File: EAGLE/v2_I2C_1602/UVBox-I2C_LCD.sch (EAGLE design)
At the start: 56 parts, among them IC1 ULN2003AD, Q1 16M, Q2 BC817, SW1 Start, SW2 Mode, SW3 Add, SW4 Sub, U1 7812DT, U2 7805DT

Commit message: 細微修改
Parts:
- added C12: 104, rcl:C-EUC0603
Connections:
- net N$29 renamed IC2P3
- removed net N$14: LCD.A, Q2.C
- new net LCD_A: LCD.A, Q2.E
- net +5V: now also C12.2
- net GND: now also C12.1, LCD.K; no longer Q2.E, VR1.E, VR2.E
- net KEY1: now also RN1D.1; no longer RN1A.1
- net KEY2: now also RN1C.1; no longer RN1B.1
- net KEY3: now also RN1B.1; no longer RN1C.1
- net KEY4: now also RN1A.1; no longer RN1D.1
- net N$12: now also Q2.C; no longer LCD.K
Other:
- moved on the sheet: C8, LCD, Q2, RN1A, RN1B, RN1C, RN1D, RN3A, VR1, VR2

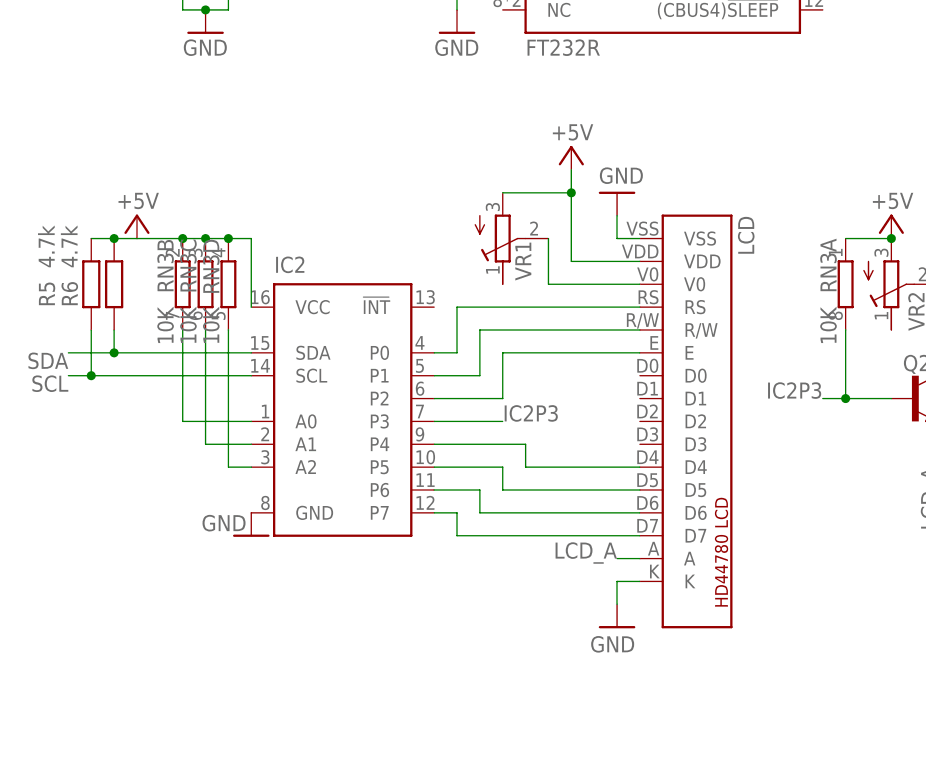
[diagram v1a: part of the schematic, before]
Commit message: 調整線路配置
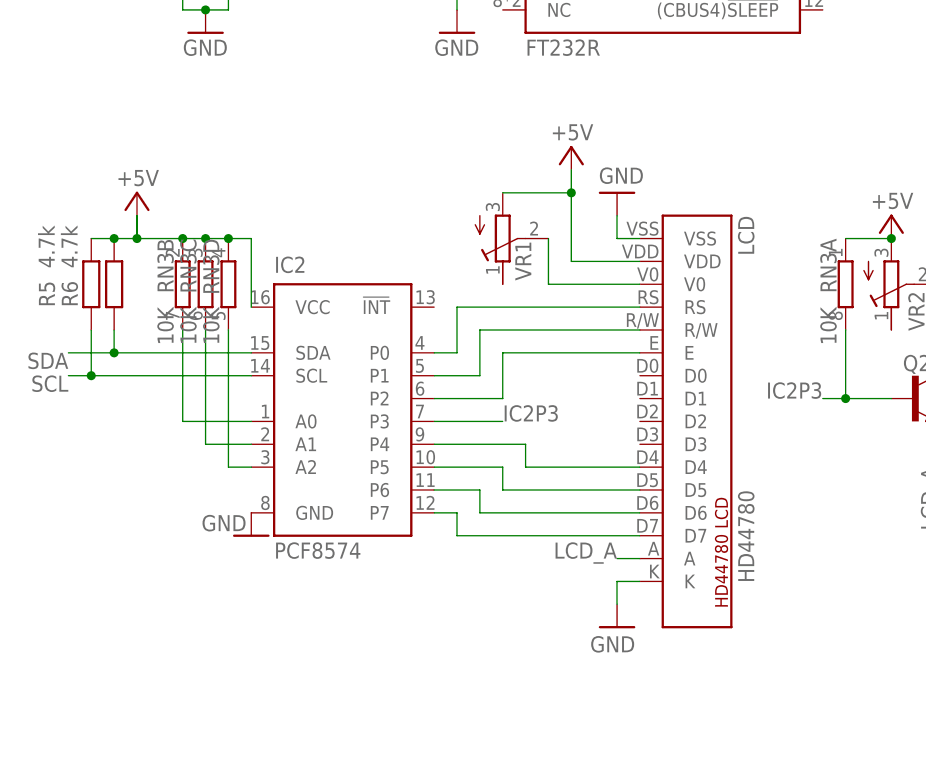
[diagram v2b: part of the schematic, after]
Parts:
- IC2: value (none) -> PCF8574
- LCD: value (none) -> HD44780
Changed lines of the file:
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@@
 <?xml version="1.0" encoding="utf-8"?>
 <!DOCTYPE eagle SYSTEM "eagle.dtd">
-<eagle version="8.4.2">
+<eagle version="8.5.2">
 <drawing>
 <settings>
-<setting alwaysvectorfont="yes"/>
+<setting alwaysvectorfont="no"/>
 <setting keepoldvectorfont="yes"/>
 <setting verticaltext="up"/>
@@
 <grid distance="0.1" unitdist="inch" unit="inch" style="lines" multiple="1" display="no" altdistance="0.01" altunitdist="inch" altunit="inch"/>
 <layers>
-<layer number="1" name="Top" color="4" fill="1" visible="yes" active="no"/>
-<layer number="2" name="Route2" color="1" fill="3" visible="yes" active="no"/>
-<layer number="3" name="Route3" color="4" fill="3" visible="yes" active="no"/>
-<layer number="4" name="Route4" color="1" fill="4" visible="yes" active="no"/>
-<layer number="5" name="Route5" color="4" fill="4" visible="yes" active="no"/>
-<layer number="6" name="Route6" color="1" fill="8" visible="yes" active="no"/>
-<layer number="7" name="Route7" color="4" fill="8" visible="yes" active="no"/>
-<layer number="8" name="Route8" color="1" fill="2" visible="yes" active="no"/>
-<layer number="9" name="Route9" color="4" fill="2" visible="yes" active="no"/>
-<layer number="10" name="Route10" color="1" fill="7" visible="yes" active="no"/>
-<layer number="11" name="Route11" color="4" fill="7" visible="yes" active="no"/>
-<layer number="12" name="Route12" color="1" fill="5" visible="yes" active="no"/>
-<layer number="13" name="Route13" color="4" fill="5" visible="yes" active="no"/>
-<layer number="14" name="Route14" color="1" fill="6" visible="yes" active="no"/>
-<layer number="15" name="Route15" color="4" fill="6" visible="yes" active="no"/>
-<layer number="16" name="Bottom" color="1" fill="1" visible="yes" active="no"/>
-<layer number="17" name="Pads" color="2" fill="1" visible="yes" active="no"/>
-<layer number="18" name="Vias" color="2" fill="1" visible="yes" active="no"/>
-<layer number="19" name="Unrouted" color="6" fill="1" visible="yes" active="no"/>
-<layer number="20" name="Dimension" color="15" fill="1" visible="yes" active="no"/>
-<layer number="21" name="tPlace" color="7" fill="1" visible="yes" active="no"/>
-<layer number="22" name="bPlace" color="7" fill="1" visible="yes" active="no"/>
-<layer number="23" name="tOrigins" color="15" fill="1" visible="yes" active="no"/>
-<layer number="24" name="bOrigins" color="15" fill="1" visible="yes" active="no"/>
-<layer number="25" name="tNames" color="7" fill="1" visible="yes" active="no"/>
-<layer number="26" name="bNames" color="7" fill="1" visible="yes" active="no"/>
-<layer number="27" name="tValues" color="7" fill="1" visible="yes" active="no"/>
-<layer number="28" name="bValues" color="7" fill="1" visible="yes" active="no"/>
+<layer number="1" name="Top" color="4" fill="1" visible="no" active="no"/>
+<layer number="2" name="Route2" color="1" fill="3" visible="no" active="no"/>
+<layer number="3" name="Route3" color="4" fill="3" visible="no" active="no"/>
+<layer number="4" name="Route4" color="1" fill="4" visible="no" active="no"/>
+<layer number="5" name="Route5" color="4" fill="4" visible="no" active="no"/>
+<layer number="6" name="Route6" color="1" fill="8" visible="no" active="no"/>
+<layer number="7" name="Route7" color="4" fill="8" visible="no" active="no"/>
+<layer number="8" name="Route8" color="1" fill="2" visible="no" active="no"/>
+<layer number="9" name="Route9" color="4" fill="2" visible="no" active="no"/>
+<layer number="10" name="Route10" color="1" fill="7" visible="no" active="no"/>
+<layer number="11" name="Route11" color="4" fill="7" visible="no" active="no"/>
+<layer number="12" name="Route12" color="1" fill="5" visible="no" active="no"/>
+<layer number="13" name="Route13" color="4" fill="5" visible="no" active="no"/>
+<layer number="14" name="Route14" color="1" fill="6" visible="no" active="no"/>
+<layer number="15" name="Route15" color="4" fill="6" visible="no" active="no"/>
+<layer number="16" name="Bottom" color="1" fill="1" visible="no" active="no"/>
+<layer number="17" name="Pads" color="2" fill="1" visible="no" active="no"/>
+<layer number="18" name="Vias" color="2" fill="1" visible="no" active="no"/>
+<layer number="19" name="Unrouted" color="6" fill="1" visible="no" active="no"/>
+<layer number="20" name="Dimension" color="15" fill="1" visible="no" active="no"/>
+<layer number="21" name="tPlace" color="7" fill="1" visible="no" active="no"/>
+<layer number="22" name="bPlace" color="7" fill="1" visible="no" active="no"/>
+<layer number="23" name="tOrigins" color="15" fill="1" visible="no" active="no"/>
+<layer number="24" name="bOrigins" color="15" fill="1" visible="no" active="no"/>
+<layer number="25" name="tNames" color="7" fill="1" visible="no" active="no"/>
+<layer number="26" name="bNames" color="7" fill="1" visible="no" active="no"/>
+<layer number="27" name="tValues" color="7" fill="1" visible="no" active="no"/>
+<layer number="28" name="bValues" color="7" fill="1" visible="no" active="no"/>
 <layer number="29" name="tStop" color="7" fill="3" visible="no" active="no"/>
 <layer number="30" name="bStop" color="7" fill="6" visible="no" active="no"/>
@@
 <layer number="35" name="tGlue" color="7" fill="4" visible="no" active="no"/>
 <layer number="36" name="bGlue" color="7" fill="5" visible="no" active="no"/>
-<layer number="37" name="tTest" color="7" fill="1" visible="yes" active="no"/>
-<layer number="38" name="bTest" color="7" fill="1" visible="yes" active="no"/>
+<layer number="37" name="tTest" color="7" fill="1" visible="no" active="no"/>
+<layer number="38" name="bTest" color="7" fill="1" visible="no" active="no"/>
 <layer number="39" name="tKeepout" color="4" fill="11" visible="no" active="no"/>
 <layer number="40" name="bKeepout" color="1" fill="11" visible="no" active="no"/>
@@
 <layer number="44" name="Drills" color="7" fill="1" visible="no" active="no"/>
 <layer number="45" name="Holes" color="7" fill="1" visible="no" active="no"/>
-<layer number="46" name="Milling" color="3" fill="1" visible="yes" active="no"/>
-<layer number="47" name="Measures" color="7" fill="1" visible="yes" active="no"/>
-<layer number="48" name="Document" color="7" fill="1" visible="yes" active="no"/>
-<layer number="49" name="Reference" color="7" fill="1" visible="yes" active="no"/>
-<layer number="50" name="dxf" color="7" fill="1" visible="yes" active="no"/>
-<layer number="51" name="tDocu" color="7" fill="1" visible="yes" active="no"/>
-<layer number="52" name="bDocu" color="7" fill="1" visible="yes" active="no"/>
-<layer number="53" name="tGND_GNDA" color="7" fill="9" visible="yes" active="no"/>
-<layer number="54" name="bGND_GNDA" color="1" fill="9" visible="yes" active="no"/>
-<layer number="56" name="wert" color="7" fill="1" visible="yes" active="no"/>
-<layer number="57" name="tCAD" color="7" fill="1" visible="yes" active="no"/>
+<layer number="46" name="Milling" color="3" fill="1" visible="no" active="no"/>
+<layer number="47" name="Measures" color="7" fill="1" visible="no" active="no"/>
+<layer number="48" name="Document" color="7" fill="1" visible="no" active="no"/>
+<layer number="49" name="Reference" color="7" fill="1" visible="no" active="no"/>
+<layer number="50" name="dxf" color="7" fill="1" visible="no" active="no"/>
+<layer number="51" name="tDocu" color="7" fill="1" visible="no" active="no"/>
+<layer number="52" name="bDocu" color="7" fill="1" visible="no" active="no"/>
+<layer number="53" name="tGND_GNDA" color="7" fill="9" visible="no" active="no"/>
+<layer number="54" name="bGND_GNDA" color="1" fill="9" visible="no" active="no"/>
+<layer number="56" name="wert" color="7" fill="1" visible="no" active="no"/>
+<layer number="57" name="tCAD" color="7" fill="1" visible="no" active="no"/>
 <layer number="90" name="Modules" color="5" fill="1" visible="no" active="no"/>
 <layer number="91" name="Nets" color="2" fill="1" visible="yes" active="yes"/>
@@
 <part name="GND11" library="supply1" deviceset="GND" device=""/>
 <part name="D9" library="led" deviceset="LED" device="CHIPLED_1206" value="Red"/>
-<part name="LCD" library="0_MyCustom" deviceset="LCD-HD44780" device="-1602"/>
-<part name="IC2" library="0_MyIC" deviceset="PCF8574" device="/SO16W"/>
+<part name="LCD" library="0_MyCustom" deviceset="LCD-HD44780" device="-1602" value="HD44780"/>
+<part name="IC2" library="0_MyIC" deviceset="PCF8574" device="/SO16W" value="PCF8574"/>
 <part name="P+11" library="supply1" deviceset="+5V" device=""/>
 <part name="RN3" library="0_MyCustom" deviceset="RN4R" device="-CAY16" value="10K"/>
@@
 <attribute name="VALUE" x="132.334" y="97.282" size="1.778" layer="96"/>
 </instance>
-<instance part="P+1" gate="1" x="20.32" y="63.5" smashed="yes">
-<attribute name="VALUE" x="18.034" y="64.262" size="1.778" layer="96"/>
+<instance part="P+1" gate="1" x="20.32" y="66.04" smashed="yes">
+<attribute name="VALUE" x="18.034" y="66.802" size="1.778" layer="96"/>
 </instance>
 <instance part="P+10" gate="1" x="246.38" y="91.44" smashed="yes">
@@
 <pinref part="R6" gate="G$1" pin="1"/>
 <wire x1="17.78" y1="60.96" x2="20.32" y2="60.96" width="0.1524" layer="91"/>
+<wire x1="20.32" y1="60.96" x2="20.32" y2="63.5" width="0.1524" layer="91"/>
 <junction x="17.78" y="60.96"/>
 <pinref part="R5" gate="G$1" pin="1"/>
@@
 <junction x="30.48" y="60.96"/>
 <wire x1="25.4" y1="60.96" x2="20.32" y2="60.96" width="0.1524" layer="91"/>
+<wire x1="20.32" y1="60.96" x2="20.32" y2="63.5" width="0.1524" layer="91"/>
 <junction x="25.4" y="60.96"/>
-</segment>
-<segment>
+<junction x="20.32" y="60.96"/>
+</segment>
+<segment>

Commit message: 更換零件與微調線路
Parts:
- removed D9: Red, led:LEDCHIPLED_1206
- added ACT: Red, led:LEDCHIPLED_0805
- PWR, RX, TX: device led:LEDCHIPLED_1206 -> led:LEDCHIPLED_0805
- RESET: value SW-PUSH/4*4*3.8MM -> SW-PUSH/3*6*4.3MM; device 0_MyCustom:SW-PUSH/4*4*3.8MM -> 0_MyCustom:SW-PUSH/3*6*4.3MM
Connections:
- net N$1 renamed VD
- net N$11 renamed D-
- net N$13 renamed RS
- net N$15 renamed D+
- net N$19 renamed !TXLED
- net N$20 renamed !RXLED
- net N$22 renamed PB1
- net N$23 renamed R/W
- net N$24 renamed E
- net N$5 renamed !RESET
- net N$6 renamed A2
- net N$61 renamed XTAL2
- net N$7 renamed A1
- net N$8 renamed A0
- net N$9 renamed XTAL1
- removed net N$21: D9.A, R10.2
- new net ACT_LED: ACT.A, R10.2
- net GND: now also ACT.C; no longer D9.C
